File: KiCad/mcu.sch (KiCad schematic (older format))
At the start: 34 parts, among them J13 SWD, J14 SDCARD, U3 STM32F407VGTx, Y1 16M

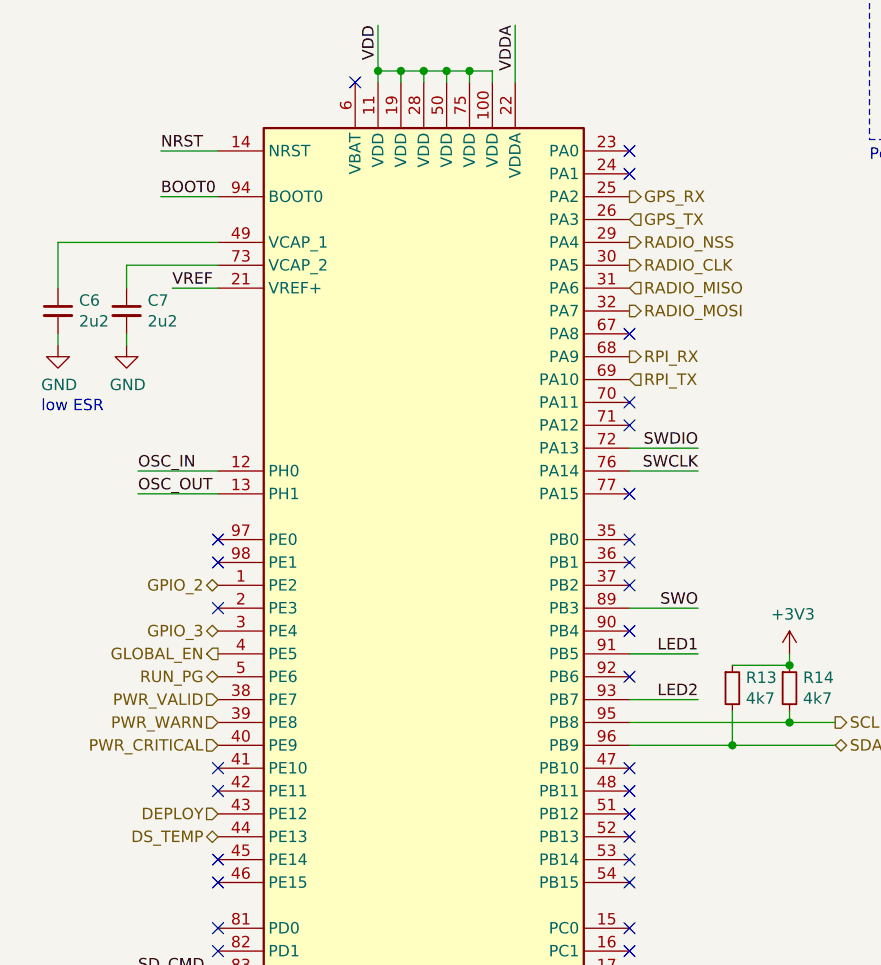
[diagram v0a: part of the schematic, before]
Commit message: Added a button and a buzzer
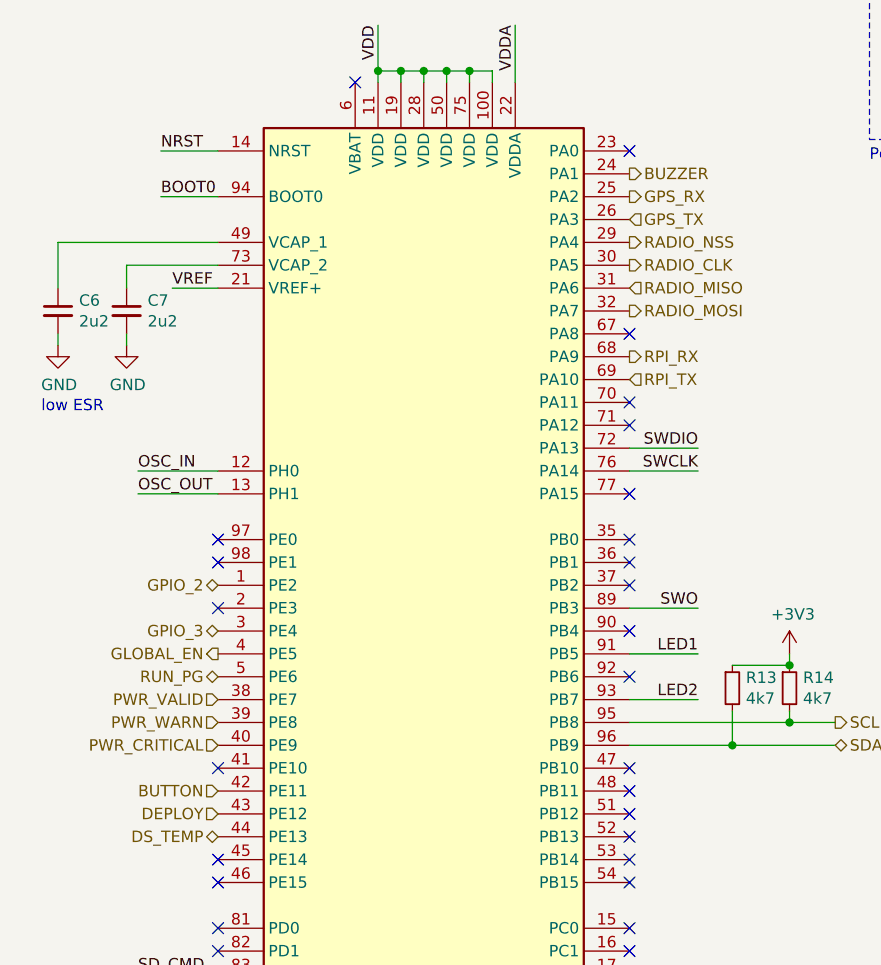
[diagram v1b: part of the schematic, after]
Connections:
- net BUZZER: now reaches U3.24 (PA1)
- net BUTTON: now reaches U3.42 (PE11)
- no-connect marks 55 -> 53
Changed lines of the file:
@@
 NoConn ~ 1650 3550
 NoConn ~ 3450 2950
-NoConn ~ 1650 4550
 NoConn ~ 1650 3750
 NoConn ~ 1650 4950
@@
 NoConn ~ 3450 3450
 NoConn ~ 3450 2850
-NoConn ~ 3450 1850
+Text HLabel 3450 1850 2    50   Output ~ 0
+BUZZER
+Text HLabel 1650 4550 0    50   Input ~ 0
+BUTTON
 $EndSCHEMATC

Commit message: Dirty production PCBs commit
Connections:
- net ACC_INT2: now reaches U3.51 (PB12)
- net ACC_INT1: now reaches U3.52 (PB13)
- no-connect marks 53 -> 51
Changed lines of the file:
@@
 NoConn ~ 3450 4450
 NoConn ~ 3450 4550
-NoConn ~ 3450 4650
 NoConn ~ 3450 4950
 NoConn ~ 3450 5450
@@
 $EndComp
 NoConn ~ 3450 4850
-NoConn ~ 3450 4750
 Text Label 3750 3050 2    50   ~ 0
 SWDIO
@@
 Text HLabel 1650 4550 0    50   Input ~ 0
 BUTTON
+Text HLabel 3450 4650 2    50   Input ~ 0
+ACC_INT2
+Text HLabel 3450 4750 2    50   Input ~ 0
+ACC_INT1
 $EndSCHEMATC
